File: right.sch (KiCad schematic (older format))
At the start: 82 parts, among them J10 UTC16-G, J18 Conn_01x01, J19 Conn_01x01, J20 Conn_01x01, J21 Conn_01x01, J22 Conn_01x01, J23 Conn_01x01, J24 Conn_01x01, J4 reset, J5 Buzzer, J6 ISP, J8 Conn_01x01, P6 WS2812, P8 SJ-43514-SMT, SW25 Socket, SW26 Socket, SW27 Socket, SW28 Socket, SW29 Socket, SW30 Socket, SW31 Socket, SW32 Socket, SW33 Socket, SW34 Socket, SW35 Socket, SW36 Socket, SW37 Socket, SW38 Socket, SW39 Socket, SW40 Socket, SW41 Socket, SW42 Socket, SW43 Socket, SW44 Socket, SW45 Socket, SW46 Socket, SW47 Socket, SW48 Socket, SW50 FSMSM, U2 ATMega32U4, Y2 16MHz

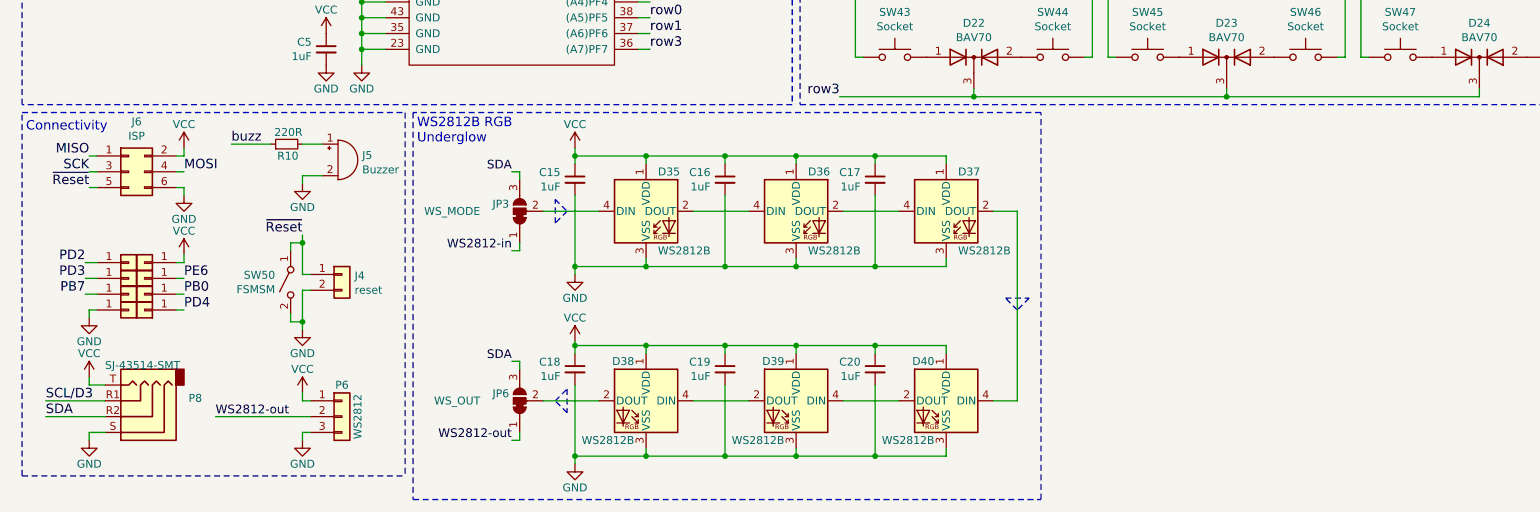
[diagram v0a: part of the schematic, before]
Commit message: Added footprint for AST1109MLTRQ buzzer
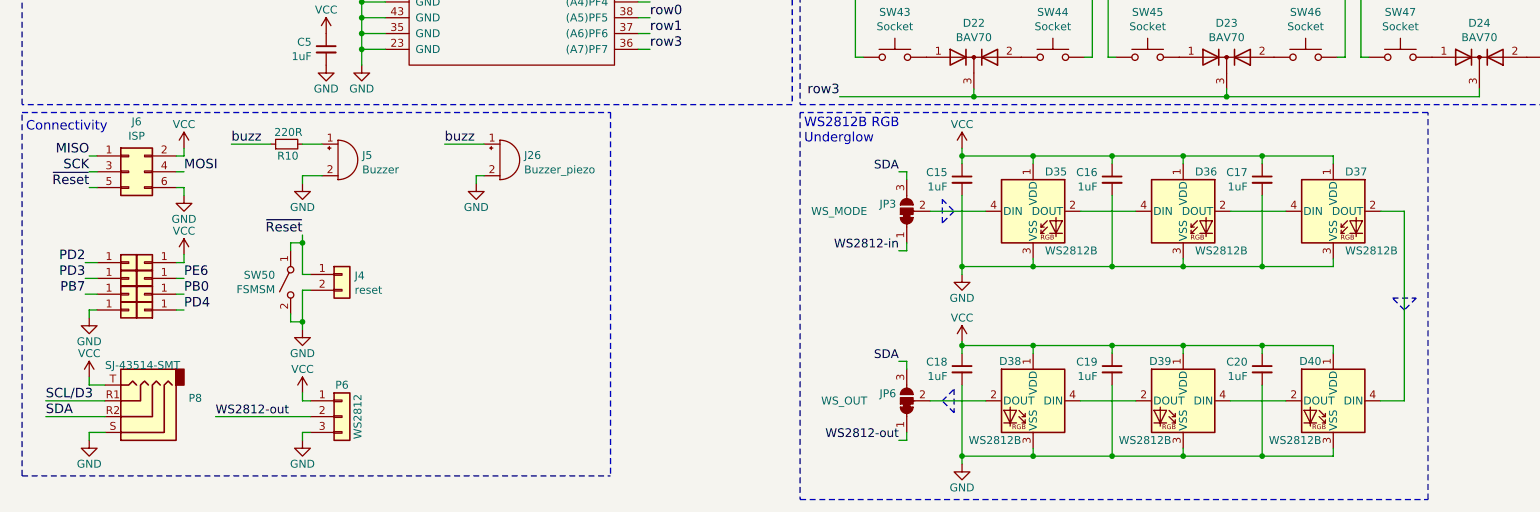
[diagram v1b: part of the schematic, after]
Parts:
- added J26: Buzzer_piezo, Buzzer_Beeper:Buzzer_Mallory_AST1109MLTRQ, symbol Device:Buzzer
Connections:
- net GND: now also J26.2 (+)
- net buzz: now also J26.1 (-)
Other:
- moved on the sheet: C15, C16, C17, C18, C19, C20, D35, D36, D37, D38, D39, D40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

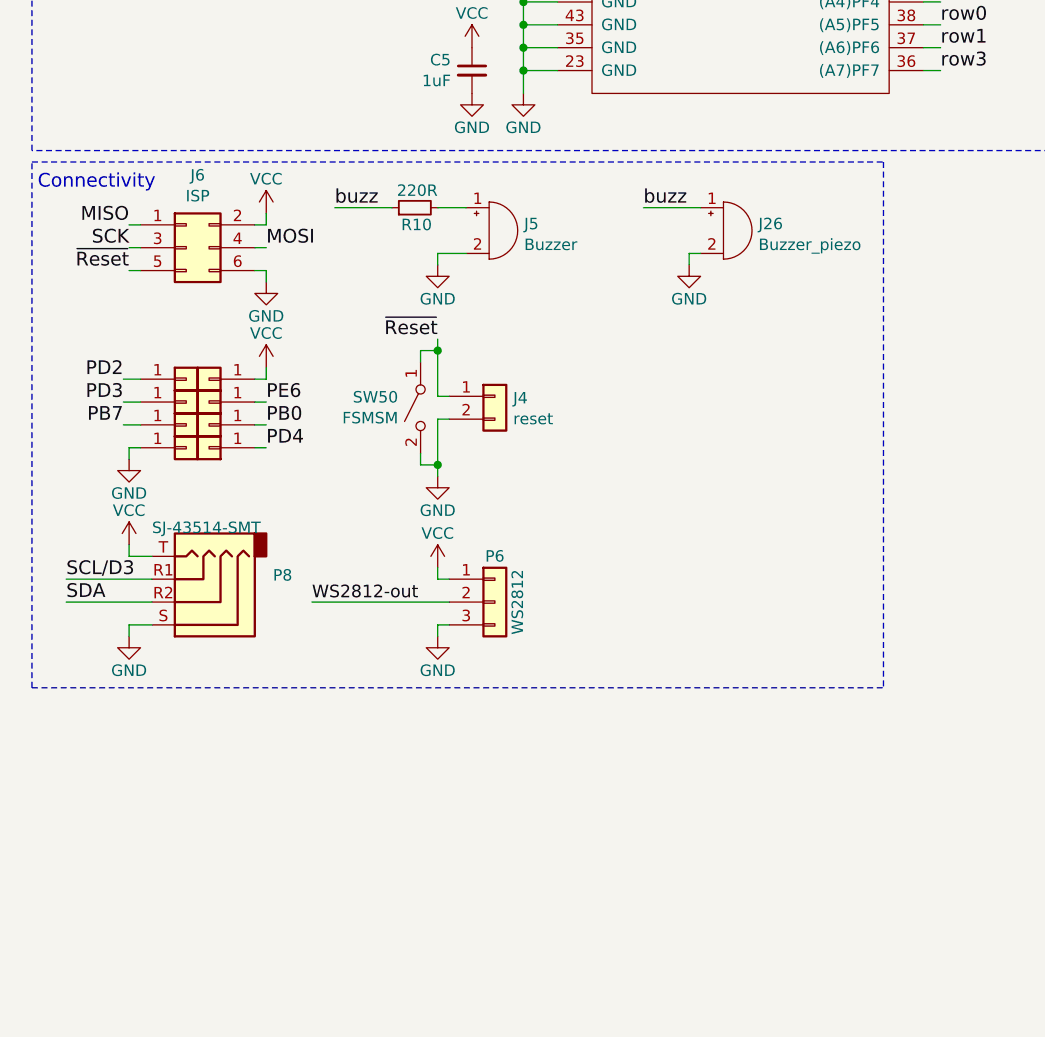
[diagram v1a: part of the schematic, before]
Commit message: Added ESD protection to connectors
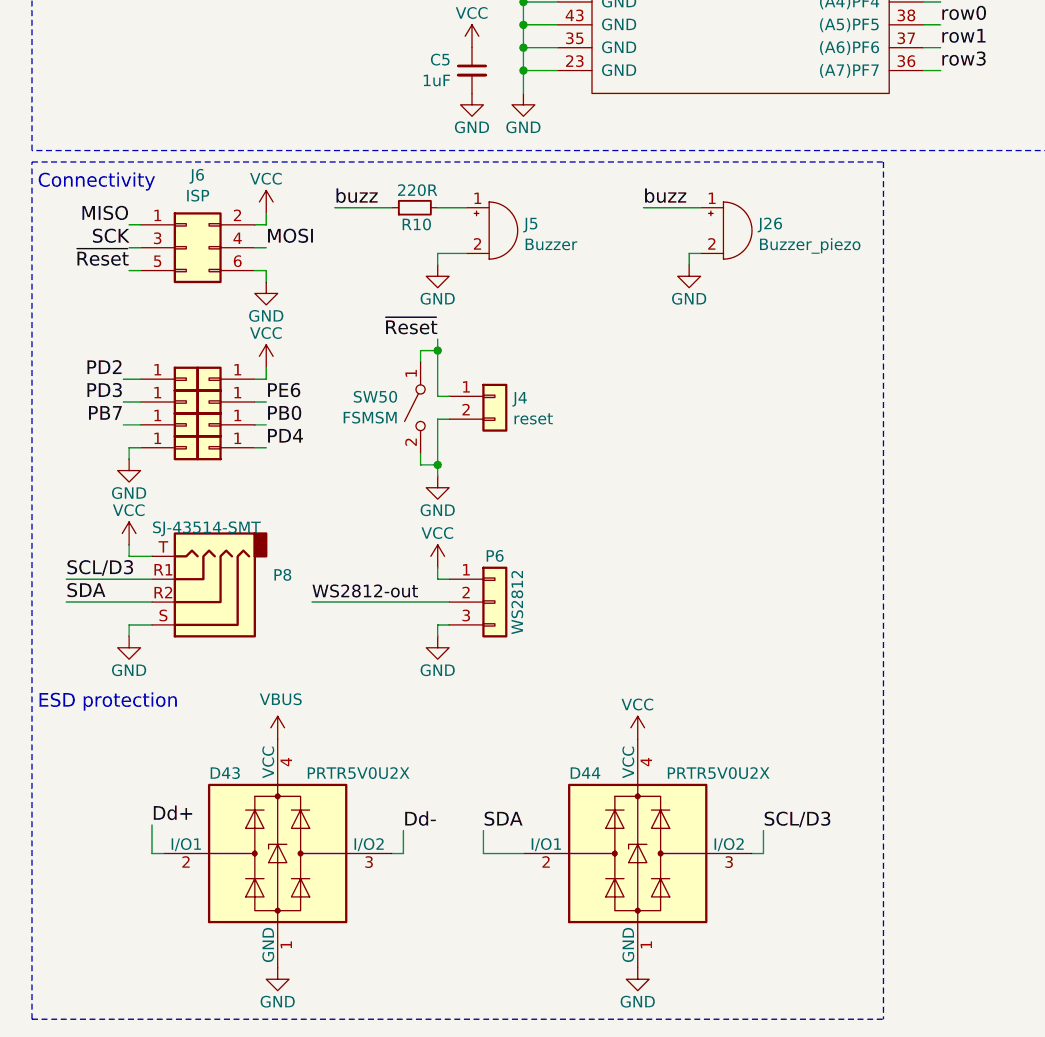
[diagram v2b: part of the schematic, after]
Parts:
- added D43, D44: PRTR5V0U2X, Package_TO_SOT_SMD:SOT-143, symbol Power_Protection:PRTR5V0U2X
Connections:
- net Dd+: now also D43.2 (I/O1)
- net Dd-: now also D43.3 (I/O2)
- net GND: now also D43.1 (GND), D44.1 (GND)
- net SCL/D3: now also D44.3 (I/O2)
- net SDA: now also D44.2 (I/O1)
- net VBUS: now also D43.4 (VCC)
- net VCC: now also D44.4 (VCC)
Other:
- note added: "ESD protection"
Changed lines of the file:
@@
 SCL/D3
 Wire Notes Line
-	875  6300 875  4000
+	875  7750 875  4000
 Wire Notes Line
 	875  4000 4600 4000
 Wire Notes Line
-	4600 4000 4600 6300
+	4600 4000 4600 7750
 Wire Notes Line
-	875  6300 4600 6300
+	875  7750 4600 7750
 Text Notes 900  4125 0    60   ~ 0
 Connectivity
@@
 	1    0    0    -1
 $EndComp
+$Comp
+L Power_Protection:PRTR5V0U2X D?
+U 1 1 5DC29991
+P 1950 7025
+AR Path="/5A0DE9BD/5DC29991" Ref="D?"  Part="1"
+AR Path="/5A0DF911/5DC29991" Ref="D43"  Part="1"
+F 0 "D43" H 1650 7375 50  0000 L CNN
+F 1 "PRTR5V0U2X" H 2075 7375 50  0000 L CNN
+F 2 "Package_TO_SOT_SMD:SOT-143" H 2010 7025 50  0001 C CNN
+F 3 "https://assets.nexperia.com/documents/data-sheet/PRTR5V0U2X.pdf" H 2010 7025 50  0001 C CNN
+	1    1950 7025
+	1    0    0    -1
+$EndComp
+$Comp
+L power:VBUS #PWR?
+U 1 1 5DC29997
+P 1950 6525
+AR Path="/5A0DE9BD/5DC29997" Ref="#PWR?"  Part="1"
+AR Path="/5A0DF911/5DC29997" Ref="#PWR0133"  Part="1"
+F 0 "#PWR0133" H 1950 6375 50  0001 C CNN
+F 1 "VBUS" H 1965 6698 50  0000 C CNN
+F 2 "" H 1950 6525 50  0001 C CNN
+F 3 "" H 1950 6525 50  0001 C CNN
+	1    1950 6525
+	1    0    0    -1
+$EndComp
+$Comp
+L power:GND #PWR?
+U 1 1 5DC2999D
+P 1950 7525
+AR Path="/5A0DE9BD/5DC2999D" Ref="#PWR?"  Part="1"
+AR Path="/5A0DF911/5DC2999D" Ref="#PWR0134"  Part="1"
+F 0 "#PWR0134" H 1950 7275 50  0001 C CNN
+F 1 "GND" H 1950 7375 50  0000 C CNN
+F 2 "" H 1950 7525 50  0000 C CNN
+F 3 "" H 1950 7525 50  0000 C CNN
+	1    1950 7525
+	-1   0    0    -1
+$EndComp
+Wire Wire Line
+	1450 7025 1400 7025
+Wire Wire Line
+	1400 7025 1400 6900
+Wire Wire Line
+	2450 7025 2500 7025
+Wire Wire Line
+	2500 7025 2500 6925
+Text Label 2500 6925 0    60   ~ 0
+Dd-
+Text Label 1400 6900 0    60   ~ 0
+Dd+
+$Comp
+L Power_Protection:PRTR5V0U2X D44
+U 1 1 5DE95F68
+P 3525 7025
+F 0 "D44" H 3225 7375 50  0000 L CNN
+F 1 "PRTR5V0U2X" H 3650 7375 50  0000 L CNN
+F 2 "Package_TO_SOT_SMD:SOT-143" H 3585 7025 50  0001 C CNN
+F 3 "https://assets.nexperia.com/documents/data-sheet/PRTR5V0U2X.pdf" H 3585 7025 50  0001 C CNN
+	1    3525 7025
+	1    0    0    -1
+$EndComp
+$Comp
+L power:GND #PWR0138
+U 1 1 5DE95F74
+P 3525 7525
+F 0 "#PWR0138" H 3525 7275 50  0001 C CNN
+F 1 "GND" H 3525 7375 50  0000 C CNN
+F 2 "" H 3525 7525 50  0000 C CNN
+F 3 "" H 3525 7525 50  0000 C CNN
+	1    3525 7525
+	-1   0    0    -1
+$EndComp
+Wire Wire Line
+	4025 7025 4075 7025
+Wire Wire Line
+	4075 7025 4075 6925
+Text Label 2850 6925 0    60   ~ 0
+SDA
+Text Label 4075 6925 0    60   ~ 0
+SCL/D3
+Wire Wire Line
+	2850 7025 2850 6925
+Wire Wire Line
+	2850 7025 3025 7025
+Text Notes 900  6400 0    60   ~ 0
+ESD protection
+$Comp
+L power:VCC #PWR?
+U 1 1 5DF2126A
+P 3525 6525
+AR Path="/5A0DE9BD/5DF2126A" Ref="#PWR?"  Part="1"
+AR Path="/5A0DF911/5DF2126A" Ref="#PWR0137"  Part="1"
+F 0 "#PWR0137" H 3525 6375 50  0001 C CNN
+F 1 "VCC" H 3525 6675 50  0000 C CNN
+F 2 "" H 3525 6525 50  0000 C CNN
+F 3 "" H 3525 6525 50  0000 C CNN
+	1    3525 6525
+	1    0    0    -1
+$EndComp

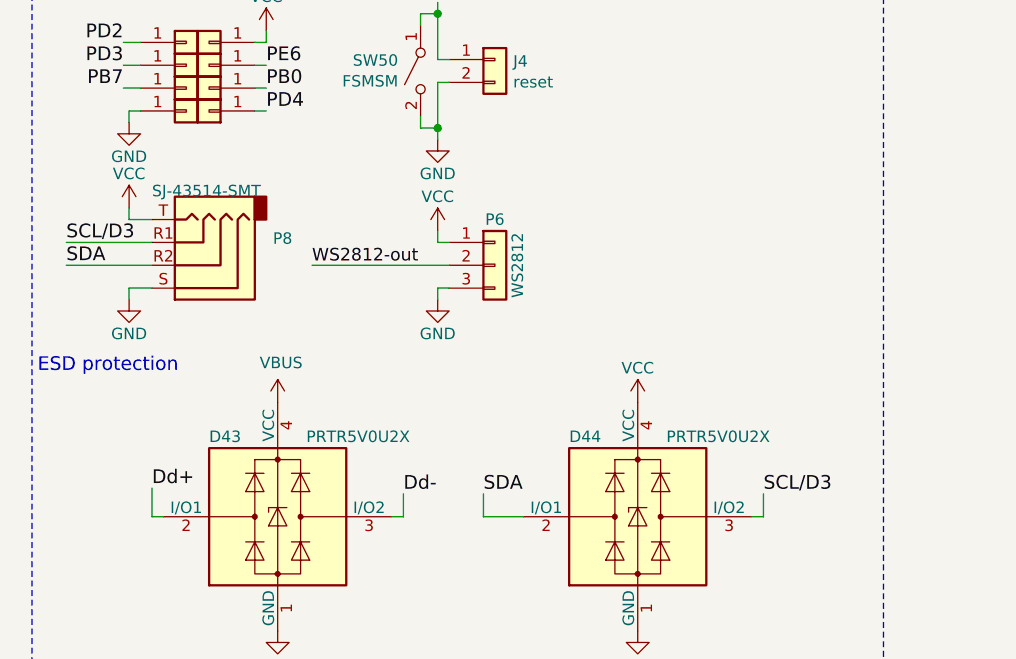
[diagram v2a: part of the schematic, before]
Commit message: Added series resistors on TRRS
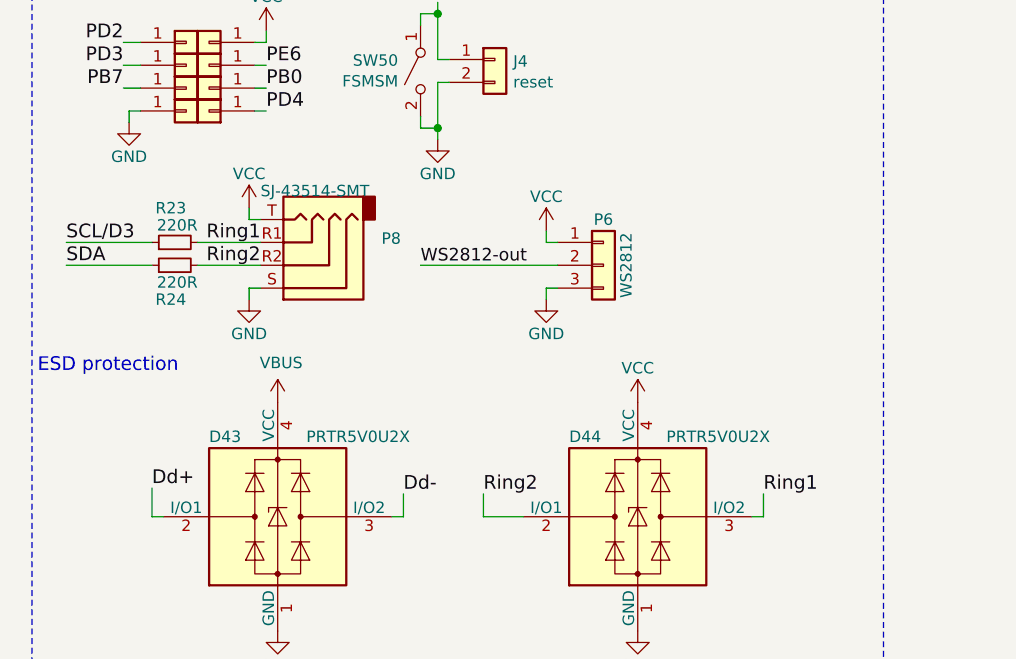
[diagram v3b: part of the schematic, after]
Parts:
- added R23, R24: 220R, Resistor_SMD:R_0603_1608Metric, symbol Device:R_Small
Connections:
- net SCL/D3: now also R23.1; no longer D44.3 (I/O2), P8.R1
- net SDA: now also R24.1; no longer D44.2 (I/O1), P8.R2
- new net Ring1: D44.3 (I/O2), P8.R1, R23.2
- new net Ring2: D44.2 (I/O1), P8.R2, R24.2
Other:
- moved on the sheet: P6, P8
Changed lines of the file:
@@
 L Connector_Generic:Conn_01x03 P6
 U 1 1 5A0E2964
-P 2900 5925
-F 0 "P6" H 2900 6125 50  0000 C CNN
-F 1 "WS2812" V 3000 5925 50  0000 C CNN
-F 2 "Wirepads:SMD_PAD_1x03_Pitch2.54mm" H 2900 5925 50  0001 C CNN
-F 3 "" H 2900 5925 50  0000 C CNN
-	1    2900 5925
+P 3375 5925
+F 0 "P6" H 3375 6125 50  0000 C CNN
+F 1 "WS2812" V 3475 5925 50  0000 C CNN
+F 2 "Wirepads:SMD_PAD_1x03_Pitch2.54mm" H 3375 5925 50  0001 C CNN
+F 3 "" H 3375 5925 50  0000 C CNN
+	1    3375 5925
 	1    0    0    -1
 $EndComp
@@
 L Connector:AudioJack4 P8
 U 1 1 5C8C7D82
-P 1600 5925
-F 0 "P8" H 1271 5808 50  0000 R CNN
-F 1 "SJ-43514-SMT" H 1800 5600 50  0000 R CNN
-F 2 "UJ31-CH-31-SMT-TR:SJ-4351X-SMT" H 1600 5925 50  0001 C CNN
-F 3 "~" H 1600 5925 50  0001 C CNN
-	1    1600 5925
+P 2075 5925
+F 0 "P8" H 1746 5808 50  0000 R CNN
+F 1 "SJ-43514-SMT" H 2275 5600 50  0000 R CNN
+F 2 "UJ31-CH-31-SMT-TR:SJ-4351X-SMT" H 2075 5925 50  0001 C CNN
+F 3 "~" H 2075 5925 50  0001 C CNN
+	1    2075 5925
 	-1   0    0    1
 $EndComp
@@
 L power:VCC #PWR?
 U 1 1 5DC94C73
-P 1300 5675
+P 1825 5675
 AR Path="/5A0DE9BD/5DC94C73" Ref="#PWR?"  Part="1"
 AR Path="/5A0DF911/5DC94C73" Ref="#PWR0108"  Part="1"
-F 0 "#PWR0108" H 1300 5525 50  0001 C CNN
-F 1 "VCC" H 1300 5825 50  0000 C CNN
-F 2 "" H 1300 5675 50  0000 C CNN
-F 3 "" H 1300 5675 50  0000 C CNN
-	1    1300 5675
+F 0 "#PWR0108" H 1825 5525 50  0001 C CNN
+F 1 "VCC" H 1825 5825 50  0000 C CNN
+F 2 "" H 1825 5675 50  0000 C CNN
+F 3 "" H 1825 5675 50  0000 C CNN
+	1    1825 5675
 	1    0    0    -1
 $EndComp
@@
 L power:GND #PWR?
 U 1 1 5DC94C79
-P 1300 6075
+P 1825 6075
 AR Path="/5A0DE9BD/5DC94C79" Ref="#PWR?"  Part="1"
 AR Path="/5A0DF911/5DC94C79" Ref="#PWR0109"  Part="1"
-F 0 "#PWR0109" H 1300 5825 50  0001 C CNN
-F 1 "GND" H 1300 5925 50  0000 C CNN
-F 2 "" H 1300 6075 50  0000 C CNN
-F 3 "" H 1300 6075 50  0000 C CNN
-	1    1300 6075
+F 0 "#PWR0109" H 1825 5825 50  0001 C CNN
+F 1 "GND" H 1825 5925 50  0000 C CNN
+F 2 "" H 1825 6075 50  0000 C CNN
+F 3 "" H 1825 6075 50  0000 C CNN
+	1    1825 6075
 	1    0    0    -1
 $EndComp
@@
 L power:VCC #PWR?
 U 1 1 5DC94CAD
-P 2650 5775
+P 3125 5775
 AR Path="/5A0DE9BD/5DC94CAD" Ref="#PWR?"  Part="1"
 AR Path="/5A0DF911/5DC94CAD" Ref="#PWR0113"  Part="1"
-F 0 "#PWR0113" H 2650 5625 50  0001 C CNN
-F 1 "VCC" H 2650 5925 50  0000 C CNN
-F 2 "" H 2650 5775 50  0000 C CNN
-F 3 "" H 2650 5775 50  0000 C CNN
-	1    2650 5775
+F 0 "#PWR0113" H 3125 5625 50  0001 C CNN
+F 1 "VCC" H 3125 5925 50  0000 C CNN
+F 2 "" H 3125 5775 50  0000 C CNN
+F 3 "" H 3125 5775 50  0000 C CNN
+	1    3125 5775
 	1    0    0    -1
 $EndComp
@@
 L power:GND #PWR?
 U 1 1 5DC94CB3
-P 2650 6075
+P 3125 6075
 AR Path="/5A0DE9BD/5DC94CB3" Ref="#PWR?"  Part="1"
 AR Path="/5A0DF911/5DC94CB3" Ref="#PWR0114"  Part="1"
-F 0 "#PWR0114" H 2650 5825 50  0001 C CNN
-F 1 "GND" H 2650 5925 50  0000 C CNN
-F 2 "" H 2650 6075 50  0000 C CNN
-F 3 "" H 2650 6075 50  0000 C CNN
-	1    2650 6075
+F 0 "#PWR0114" H 3125 5825 50  0001 C CNN
+F 1 "GND" H 3125 5925 50  0000 C CNN
+F 2 "" H 3125 6075 50  0000 C CNN
+F 3 "" H 3125 6075 50  0000 C CNN
+	1    3125 6075
 	1    0    0    -1
 $EndComp
@@
 	3025 3300 3175 3300
 Wire Wire Line
-	2100 5925 2700 5925
+	2575 5925 3175 5925
 Wire Wire Line
 	2650 4400 2650 4450
 Wire Wire Line
-	2650 6025 2700 6025
-Wire Wire Line
-	2650 6075 2650 6025
-Wire Wire Line
-	2650 5825 2700 5825
-Wire Wire Line
-	2650 5775 2650 5825
-Wire Wire Line
-	1300 5675 1300 5725
-Wire Wire Line
-	1300 6025 1400 6025
-Wire Wire Line
-	1300 6075 1300 6025
+	3125 6025 3175 6025
+Wire Wire Line
+	3125 6075 3125 6025
+Wire Wire Line
+	3125 5825 3175 5825
+Wire Wire Line
+	3125 5775 3125 5825
+Wire Wire Line
+	1825 5675 1825 5725
+Wire Wire Line
+	1825 6025 1875 6025
+Wire Wire Line
+	1825 6075 1825 6025
 Wire Wire Line
 	2550 775  2550 1000
@@
 	3025 3150 3025 3200
 Wire Wire Line
-	1300 5725 1400 5725
+	1825 5725 1875 5725
 Text Label 4850 3600 0    60   ~ 0
 row3
@@
 Wire Notes Line
 	6775 5900 6700 5825
-Text Label 2100 5925 0    55   ~ 0
+Text Label 2575 5925 0    55   ~ 0
 WS2812-out
 Wire Wire Line
@@
 Text Notes 900  4125 0    60   ~ 0
 Connectivity
-Wire Wire Line
-	1025 5925 1400 5925
-Wire Wire Line
-	1025 5825 1400 5825
 Text Label 1900 5150 0    60   ~ 0
 PB0
@@
 Wire Wire Line
 	4075 7025 4075 6925
-Text Label 2850 6925 0    60   ~ 0
-SDA
-Text Label 4075 6925 0    60   ~ 0
-SCL/D3
 Wire Wire Line
 	2850 7025 2850 6925
@@
 	1    0    0    -1
 $EndComp
+$Comp
+L Device:R_Small R?
+U 1 1 5DB0FA1A
+P 1500 5925
+AR Path="/5A0DE9BD/5DB0FA1A" Ref="R?"  Part="1"
+AR Path="/5A0DF911/5DB0FA1A" Ref="R24"  Part="1"
+F 0 "R24" V 1350 5875 50  0000 L CNN
+F 1 "220R" V 1425 5825 50  0000 L CNN
+F 2 "Resistor_SMD:R_0603_1608Metric" H 1500 5925 50  0001 C CNN
+F 3 "" H 1500 5925 50  0000 C CNN
+	1    1500 5925
+	0    -1   -1   0
+$EndComp
+$Comp
+L Device:R_Small R?
+U 1 1 5DB0FA20
+P 1500 5825
+AR Path="/5A0DE9BD/5DB0FA20" Ref="R?"  Part="1"
+AR Path="/5A0DF911/5DB0FA20" Ref="R23"  Part="1"
+F 0 "R23" V 1650 5775 50  0000 L CNN
+F 1 "220R" V 1575 5725 50  0000 L CNN
+F 2 "Resistor_SMD:R_0603_1608Metric" H 1500 5825 50  0001 C CNN
+F 3 "" H 1500 5825 50  0000 C CNN
+	1    1500 5825
+	0    -1   -1   0
+$EndComp
+Wire Wire Line
+	1875 5925 1600 5925
+Wire Wire Line
+	1600 5825 1875 5825
+Wire Wire Line
+	1400 5825 1025 5825
+Wire Wire Line
+	1025 5925 1400 5925
+Text Label 1875 5825 2    60   ~ 0
+Ring1
+Text Label 1875 5925 2    60   ~ 0
+Ring2
+Text Label 4075 6925 0    60   ~ 0
+Ring1
+Text Label 2850 6925 0    60   ~ 0
+Ring2
 $EndSCHEMATC

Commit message: Added PE2 pull-down for dfu
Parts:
- added R?: 100k, Resistor_SMD:R_0603_1608Metric, symbol Device:R_Small
- U2: symbol 8Bit-MCU:ATMega32U4 -> vitamins_included-rescue:ATMega32U4-8Bit-MCU
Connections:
- net GND: now also R?.2
- net col2: now also R?.1
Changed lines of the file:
@@
 EESchema Schematic File Version 4
-LIBS:vitamins_included-cache
-EELAYER 29 0
+EELAYER 30 0
 EELAYER END
 $Descr A4 11693 8268
@@
 $EndComp
 $Comp
-L 8Bit-MCU:ATMega32U4 U2
+L vitamins_included-rescue:ATMega32U4-8Bit-MCU U2
 U 1 1 5A0E298E
 P 3425 1550
@@
 Wire Wire Line
 	4775 3200 4850 3200
-Wire Wire Line
-	4775 2850 4850 2850
 Wire Wire Line
 	4775 2700 4850 2700
@@
 	5525 2500 5650 2500
 Wire Wire Line
-	5650 2500 5650 2550
-$Comp
-L power:GND #PWR?
-U 1 1 5DC94F9A
-P 5650 2550
-AR Path="/5A0DE9BD/5DC94F9A" Ref="#PWR?"  Part="1"
-AR Path="/5A0DF911/5DC94F9A" Ref="#PWR0125"  Part="1"
-F 0 "#PWR0125" H 5650 2300 50  0001 C CNN
-F 1 "GND" H 5650 2400 50  0000 C CNN
-F 2 "" H 5650 2550 50  0000 C CNN
-F 3 "" H 5650 2550 50  0000 C CNN
-	1    5650 2550
-	1    0    0    -1
-$EndComp
-Wire Wire Line
 	6825 4525 6825 4975
 Wire Wire Line
@@
 Text Label 2850 6925 0    60   ~ 0
 Ring2
+$Comp
+L Device:R_Small R?
+U 1 1 5F84799C
+P 5425 2850
+F 0 "R?" H 5450 2875 50  0000 L CNN
+F 1 "100k" H 5450 2800 50  0000 L CNN
+F 2 "Resistor_SMD:R_0603_1608Metric" H 5425 2850 50  0001 C CNN
+F 3 "" H 5425 2850 50  0000 C CNN
+	1    5425 2850
+	0    -1   1    0
+$EndComp
+$Comp
+L power:GND #PWR?
+U 1 1 5F848EE3
+P 5650 2900
+AR Path="/5A0DE9BD/5F848EE3" Ref="#PWR?"  Part="1"
+AR Path="/5A0DF911/5F848EE3" Ref="#PWR?"  Part="1"
+F 0 "#PWR?" H 5650 2650 50  0001 C CNN
+F 1 "GND" H 5650 2750 50  0000 C CNN
+F 2 "" H 5650 2900 50  0000 C CNN
+F 3 "" H 5650 2900 50  0000 C CNN
+	1    5650 2900
+	1    0    0    -1
+$EndComp
+Wire Wire Line
+	5650 2900 5650 2850
+Wire Wire Line
+	5650 2850 5525 2850
+Wire Wire Line
+	5650 2500 5650 2850
+Connection ~ 5650 2850
+Wire Wire Line
+	4775 2850 5325 2850
 $EndSCHEMATC
